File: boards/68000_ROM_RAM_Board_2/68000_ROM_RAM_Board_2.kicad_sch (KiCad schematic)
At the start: 26 parts, among them J1 RCBus_80PIN_68000, J10 Conn_01x06, J11 Conn_01x06, J12 Conn_01x06, J2 Conn_01x03, J3 Conn_01x03, J4 Conn_01x03, J5 Conn_01x03, J6 Conn_01x03, J7 Conn_01x03, J8 Conn_01x03, J9 Conn_01x03, U1 74LS125, U2 74LS139, U3 SST39SF040, U4 SST39SF040, U5 74LS138, U6 AS6C4008-55PCN, U7 AS6C4008-55PCN

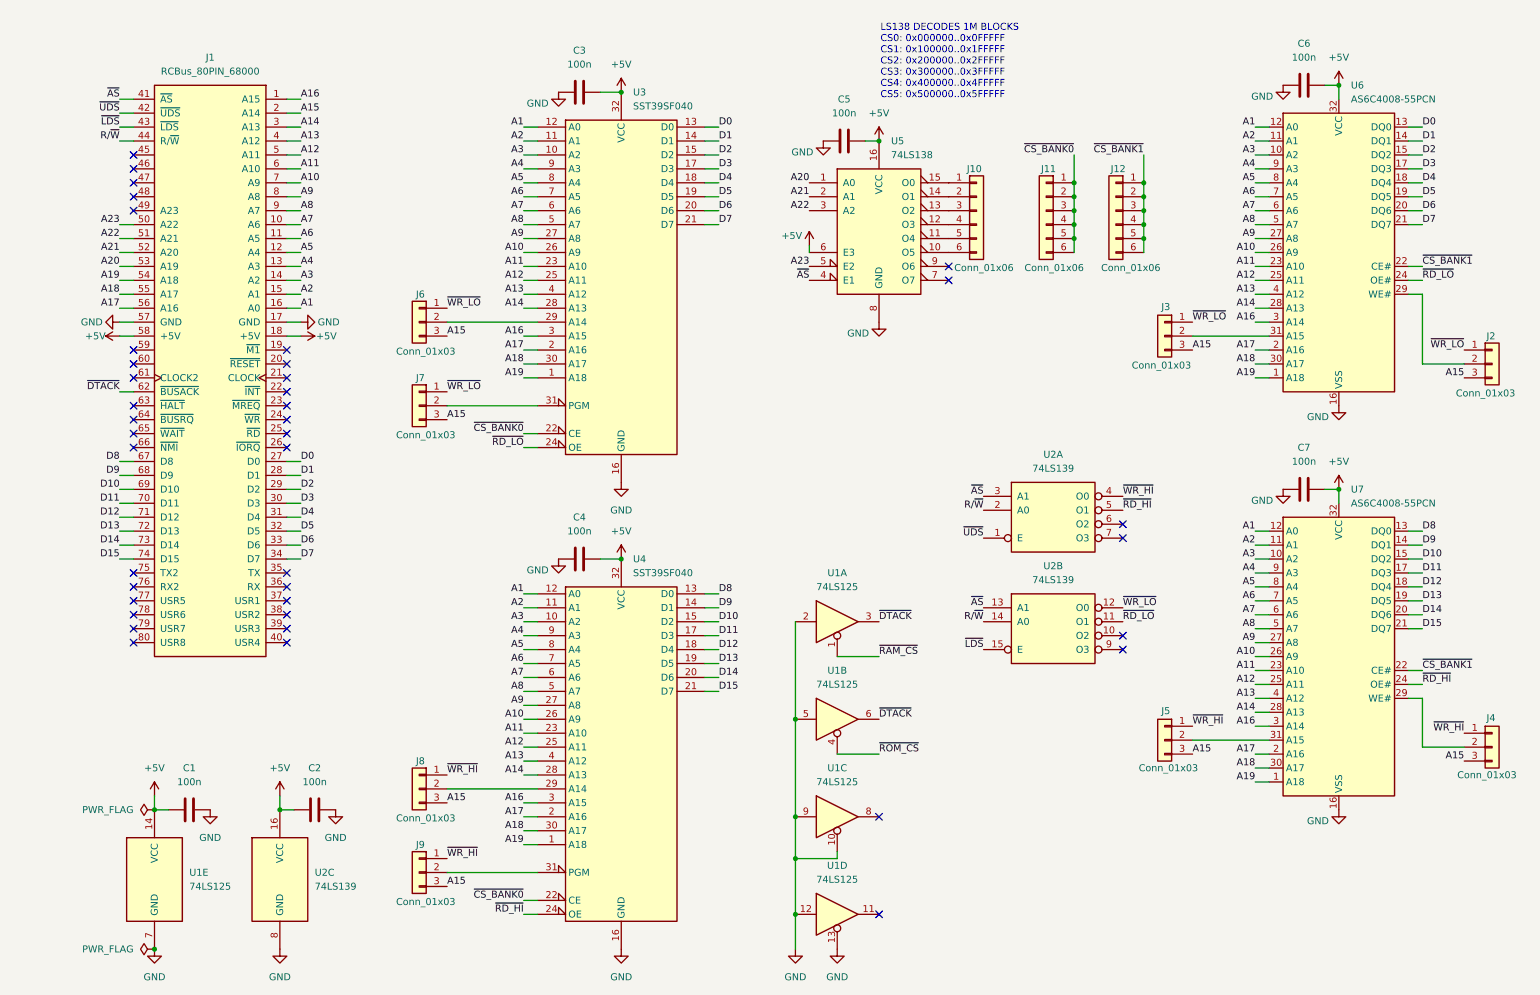
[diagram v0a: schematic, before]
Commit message: updated rom/ram board #2 schematic notes
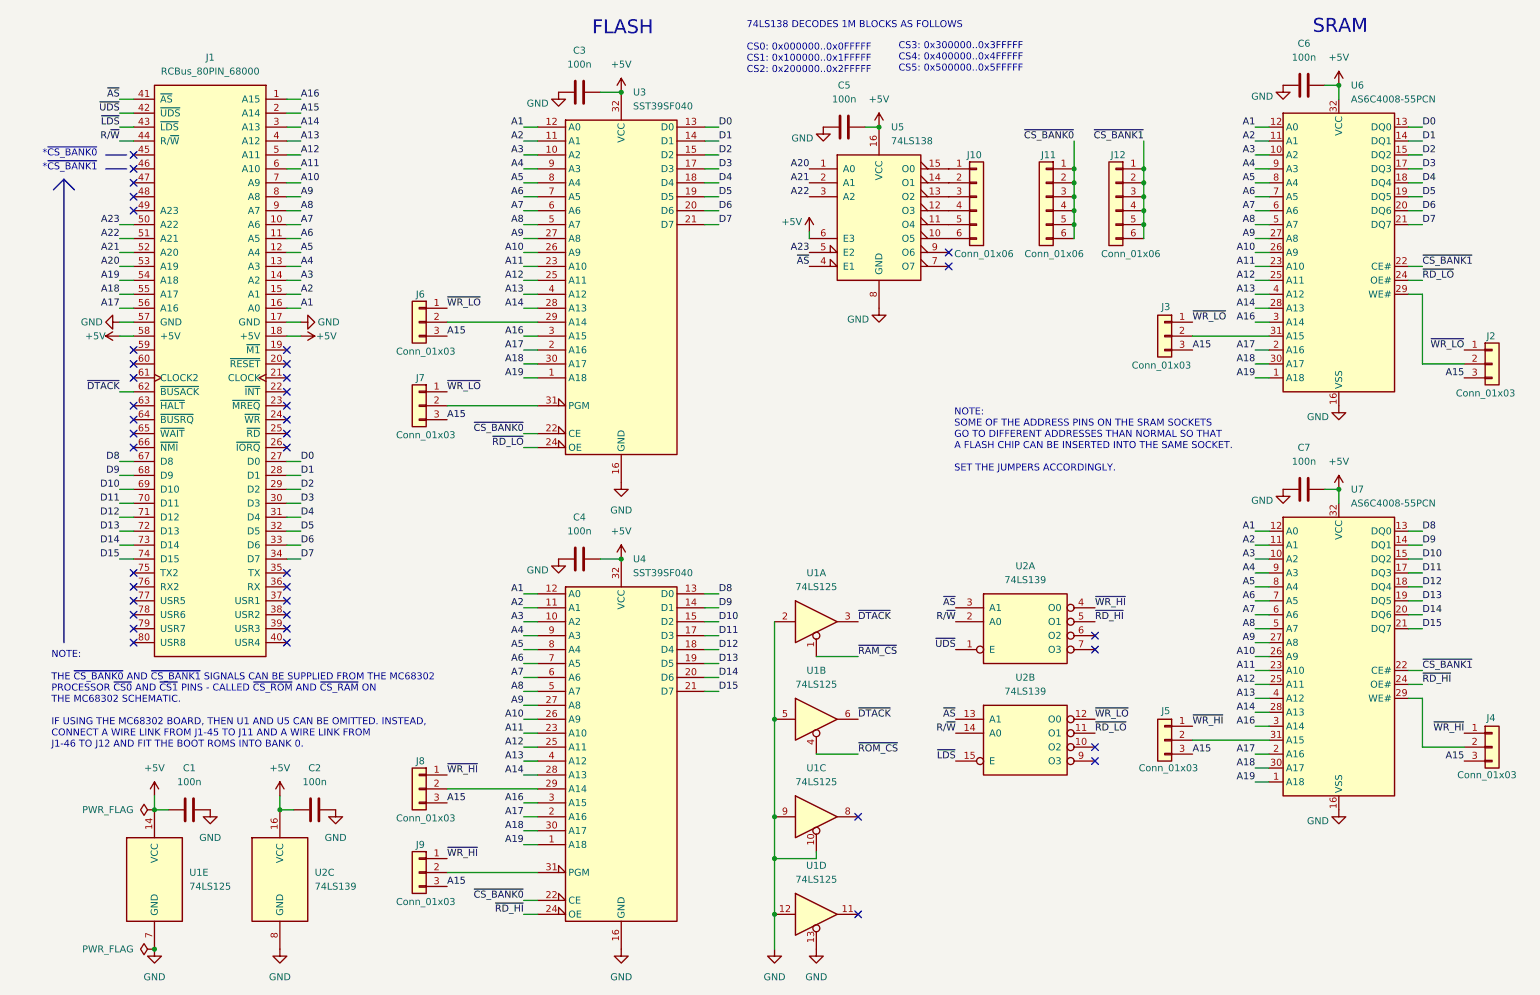
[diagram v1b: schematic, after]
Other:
- note added: "*~{CS_BANK0}"
- note added: "*~{CS_BANK1}"
- note added: "74LS138 DECODES 1M BLOCKS AS FOLLOWS CS0: 0x000000..0x0FFFFF CS1: 0x100000..0x1FFFFF CS2: 0x200000..0x2FFFFF"
- note added: "CS3: 0x300000..0x3FFFFF CS4: 0x400000..0x4FFFFF CS5: 0x500000..0x5FFFFF"
- note added: "FLASH"
- note added: "NOTE: SOME OF THE ADDRESS PINS ON THE SRAM SOCKETS GO TO DIFFERENT ADDRESSES THAN NORMAL SO THAT A FLASH CHIP CAN BE INSERTED INTO THE SAME SOCKET. SET THE JUMPERS ACCORDINGLY."
- note added: "NOTE: THE ~{CS_BANK0} AND ~{CS_BANK1} SIGNALS CAN BE SUPPLIED FROM THE MC68302 PROCESSOR ~{CS0} AND ~{CS1} PINS - CALLED ~{CS_ROM} AND ~{CS_RAM} ON THE MC68302 SCHEMATIC. IF USING THE MC68302 BOARD, THEN U1 AND U5 CAN BE OMITTED. INSTEAD, CONNECT A WIRE LINK FROM J1-45 TO J11 AND A WIRE LINK FROM J1-46 TO J12 AND FIT THE BOOT ROMS INTO BANK 0."
- note added: "SRAM"
- note removed: "LS138 DECODES 1M BLOCKS CS0: 0x000000..0x0FFFFF CS1: 0x100000..0x1FFFFF CS2: 0x200000..0x2FFFFF CS3: 0x300000..0x3FFFFF CS4: 0x400000..0x4FFFFF CS5: 0x500000..0x5FFFFF"
- moved on the sheet: C5, J10, J11, J12, U1A, U1B, U1C, U1D, U2A, U2B, U5
